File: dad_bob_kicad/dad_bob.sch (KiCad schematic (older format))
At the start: 10 parts, among them J1_BNC1 BNC5-J-P-GN-RA-BH2D, J2_BLACK1 Conn_01x01, J3_RED1 Conn_01x01, T1 GT07-110-013, U1 SL1002A600SP

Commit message: Imported HPF, added divider, dad IO, & relay
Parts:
- added C?: CP, symbol Device:CP
- added D? (x2): 1N4001, Diode_THT:D_DO-41_SOD81_P10.16mm_Horizontal, symbol Diode:1N4001
- added J1, J2: Conn_01x01, symbol Connector_Generic:Conn_01x01
- added J? (x2): analog_discovery_IO, symbol Connector_Generic:analog_discovery_IO
- added K?: EC2-5NU, Relay_THT:Relay_DPDT_Kemet_EC2, symbol Relay:EC2-5NU
- added Q?: 2N2219, Package_TO_SOT_THT:TO-39-3, symbol Transistor_BJT:2N2219
- added R? (x5): 1M, symbol Device:R
- added R?: 50k, symbol Device:R
- added R?: 1k, symbol Device:R
- J3: renamed from J2_BLACK1; footprint Connector_Coaxial:SMA_Amphenol_132203-12_Horizontal -> (none)
- J4: renamed from J3_RED1; footprint Connector_Coaxial:SMA_Amphenol_132203-12_Horizontal -> (none)
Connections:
- net labels added: CV7, CV8, DIVin1+, DIVin1-, DIVout1+, DIVout1-, GND, PLCin+, PLCin-, PLCout+, PLCout-, relaypwr, scope1+, scope1-, scope2+, scope2-, waveform
- net labels removed: Out
- wire segments 41 -> 71
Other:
- moved on the sheet: C1, C2, J1_BNC1, J3, J4, RV1, T1, U1, V1

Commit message: Corrected hpf scheme, added pass throughs on the dad io, changed j1/j2 inputs
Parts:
- removed J?: analog_discovery_IO, symbol Connector_Generic:analog_discovery_IO
- added C?: CP, symbol Device:CP
- added D? (x2): 1N4001, Diode_THT:D_DO-41_SOD81_P10.16mm_Horizontal, symbol Diode:1N4001
- added J?: analog_discovery_IO, symbol Connector_Generic:analog_discovery_IO
- added K?: EC2-5NU, Relay_THT:Relay_DPDT_Kemet_EC2, symbol Relay:EC2-5NU
- added Q?: 2N2219, Package_TO_SOT_THT:TO-39-3, symbol Transistor_BJT:2N2219
- added R? (x2): 1M, symbol Device:R
- added R?: 50k, symbol Device:R
- added R?: 1k, symbol Device:R
- renumbered J1_BNC1 to J7
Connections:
- net labels added: 1, 10, 11, 12, 13, 14, 15, 2, 3, 4, 5, 8, 9, BNCin+, BNCin-, CV6, DIVin2+, DIVin2-, DIVout2+, DIVout2-, V-, trigger1, trigger2, waveform1, waveform2
- net labels removed: CV8, waveform
- wire segments 71 -> 158
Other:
- moved on the sheet: C1, C2, C?, D?, J1, J2, J3, J4, J7, J?, K?, Q?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

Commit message: Reworked voltage divider, added attenuation simulation schematic
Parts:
- removed R? (x2): 50k, symbol Device:R
- removed R? (x4): 1M, symbol Device:R
- added C? (x6): 4pf, symbol Device:C
- added C? (x4): 350pF, symbol Device:C
- added R? (x2): 50k, symbol Device:R
- added R?: DNP, symbol Device:R
- added R? (x3): 1M, symbol Device:R
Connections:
- wire segments 158 -> 183
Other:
- note added: "this tvs needs switched out"
- moved on the sheet: C1, C2, C?, D?, J1, J2, J3, J4, J7, J?, K?, Q?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

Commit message: Altered voltage divider section & added simulation circuit
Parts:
- C2: footprint Capacitor_SMD:C_0603_1608Metric_Pad1.05x0.95mm_HandSolder -> Capacitor_SMD:C_0805_2012Metric_Pad1.15x1.40mm_HandSolder
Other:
- note added: "Make C2 0806"
- note added: "this tvs needs switched out: SMCJ9.0CA"
- note removed: "this tvs needs switched out"
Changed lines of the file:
@@
 F 0 "C2" H 5122 1254 50  0000 R CNN
 F 1 "220pF" H 5122 1345 50  0000 R CNN
-F 2 "Capacitor_SMD:C_0603_1608Metric_Pad1.05x0.95mm_HandSolder" H 5300 1300 50  0001 C CNN
+F 2 "Capacitor_SMD:C_0805_2012Metric_Pad1.15x1.40mm_HandSolder" H 5300 1300 50  0001 C CNN
 F 3 "~" H 5300 1300 50  0001 C CNN
 F 4 "C" H 5300 1300 50  0001 C CNN "Spice_Primitive"
@@
 Wire Wire Line
 	2750 950  3050 950
-Text Notes 4250 1750 0    50   ~ 0
-this tvs needs switched out
 Wire Wire Line
 	1100 5600 1300 5600
@@
 Wire Wire Line
 	2400 6050 2400 6100
+Text Notes 4200 1800 0    50   ~ 0
+this tvs needs switched out: SMCJ9.0CA
+Text Notes 5450 1450 0    50   ~ 0
+Make C2 0806
 $EndSCHEMATC

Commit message: Added differential schematic & associated symbols & footprints, no values, ready for initial layout
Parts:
- removed D1: SMCJ5.0A, DIONM7959X262N, symbol SMCJ5.0A:SMCJ5.0A
- added C? (x3): 86nF, symbol Device:C
- added C? (x2): 4pf, symbol Device:C
- added C? (x2): CTRIM, symbol Device:CTRIM
- added D?: SMCJ9.0CA, DIONM7959X262N, symbol SMCJ5.0A:SMCJ9.0CA
- added J? (x3): Conn_01x03_Male, symbol Connector:Conn_01x03_Male
- added J?: BNC5-J-P-GN-RA-BH2D, BNC5-J-P-GN-RA-BH2D_kicad:BNC5JPGNRABH2D, symbol BNC5-J-P-GN-RA-BH2D:BNC5-J-P-GN-RA-BH2D
- added R? (x3): 30M, symbol Device:R
- added R? (x2): 1M, symbol Device:R
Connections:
- wire segments 183 -> 221
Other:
- note added: "BNC out for standalone"
- note added: "Made C2 0806"
- note added: "switched to: SMCJ9.0CA"
- note removed: "Make C2 0806"
- note removed: "this tvs needs switched out: SMCJ9.0CA"
- moved on the sheet: C1, C2, C?, D?, J1, J2, J3, J4, J7, K?, Q?, R?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

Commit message: Added pcbNew files, block layouts complete
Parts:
- removed J? (x2): analog_discovery_IO, symbol Connector_Generic:analog_discovery_IO
- removed J?: BNC5-J-P-GN-RA-BH2D, BNC5-J-P-GN-RA-BH2D_kicad:BNC5JPGNRABH2D, symbol BNC5-J-P-GN-RA-BH2D:BNC5-J-P-GN-RA-BH2D
- removed V1: dc 0 ac 240, symbol pspice:VSOURCE
- added J6: Conn_02x15_Odd_Even, Connector_PinHeader_2.54mm:PinHeader_2x15_P2.54mm_Horizontal, symbol Connector_Generic:Conn_02x15_Odd_Even
- added J9: Conn_02x15_Odd_Even, Connector_PinSocket_2.54mm:PinSocket_2x15_P2.54mm_Horizontal, symbol Connector_Generic:Conn_02x15_Odd_Even
- C10, C11, C12, C13, C15, C16, C18, C19, C20, C21, C3, C4, C5, C6, C7, C8, C9: renamed from C?; footprint (none) -> Capacitor_SMD:C_0805_2012Metric_Pad1.15x1.40mm_HandSolder
- C14, C17: renamed from C?; footprint (none) -> Capacitor_SMD:C_Trimmer_Voltronics_JQ
- D1: renamed from D?; footprint DIONM7959X262N -> SMCJ5:DIONM7959X262N; symbol SMCJ5.0A:SMCJ9.0CA -> 00_kyuditsky_kicad:SMCJ9.0CA
- J1, J2, J3, J4: footprint (none) -> kyuditsky_kicad_fp:Banana_Jack_S_RA_73099
- J10, J5, J8: renamed from J?; footprint (none) -> Connector_PinHeader_2.54mm:PinHeader_1x03_P2.54mm_Vertical
- J7: symbol BNC5-J-P-GN-RA-BH2D:BNC5-J-P-GN-RA-BH2D -> 00_kyuditsky_kicad:BNC5-J-P-GN-RA-BH2D
- R1, R10, R11, R12, R13, R14, R15, R16, R2, R3, R4, R5, R6, R7, R8, R9: renamed from R?; footprint (none) -> Resistor_SMD:R_0805_2012Metric_Pad1.15x1.40mm_HandSolder
- RV1: footprint CAPPM10080X500N -> VP4032K122R300_kicad:CAPPM10080X500N; symbol VP4032K122R300:VP4032K122R300 -> 00_kyuditsky_kicad:VP4032K122R300
- T1: footprint GT07-110-013-Modifed:GT07110013 -> kyuditsky_kicad_fp:GT07110013; symbol GT07-110-013:GT07-110-013 -> 00_kyuditsky_kicad:GT07-110-013
- U1: symbol SL1002A600SP:SL1002A600SP -> 00_kyuditsky_kicad:SL1002A600SP
- gave numbers to parts that had none: 8
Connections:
- net 0: now also J6.16 (Pin_16), J9.16 (Pin_16)
- net 1: now also J6.18 (Pin_18), J9.18 (Pin_18)
- net 10: now also J6.19 (Pin_19), J9.19 (Pin_19)
- net 11: now also J6.21 (Pin_21), J9.21 (Pin_21)
- net 12: now also J6.23 (Pin_23), J9.23 (Pin_23)
- net 13: now also J6.25 (Pin_25), J9.25 (Pin_25)
- net 14: now also J6.27 (Pin_27), J9.27 (Pin_27)
- net 15: now also J6.29 (Pin_29), J9.29 (Pin_29)
- net 2: now also J6.20 (Pin_20), J9.20 (Pin_20)
- net 3: now also J6.22 (Pin_22), J9.22 (Pin_22)
- net 4: now also J6.24 (Pin_24), J9.24 (Pin_24)
- net 5: now also J6.26 (Pin_26), J9.26 (Pin_26)
- net 8: now also J6.15 (Pin_15), J9.15 (Pin_15)
- net 9: now also J6.17 (Pin_17), J9.17 (Pin_17)
- net BNCin+: now also K2.3; no longer K2.5
- net BNCin-: now also K2.10; no longer K2.8
- net CV6: now also J6.28 (Pin_28), J9.28 (Pin_28)
- net CV7: now also J6.30 (Pin_30), J9.30 (Pin_30)
- net DIVout2+: now also K2.5; no longer K2.3
- net DIVout2-: now also K2.8; no longer K2.10
- net GND: now also J6.11 (Pin_11), J6.12 (Pin_12), J6.5 (Pin_5), J6.6 (Pin_6), J9.11 (Pin_11), J9.12 (Pin_12), J9.5 (Pin_5), J9.6 (Pin_6)
- net relaypwr: now also J6.8 (Pin_8), J9.8 (Pin_8)
- net scope1+: now also J6.2 (Pin_2), J9.2 (Pin_2)
- net scope1-: now also J6.1 (Pin_1), J9.1 (Pin_1)
- net scope2+: now also J6.4 (Pin_4), J9.4 (Pin_4)
- net scope2-: now also J6.3 (Pin_3), J9.3 (Pin_3)
- net trigger1: now also J6.14 (Pin_14), J9.14 (Pin_14)
- net trigger2: now also J6.13 (Pin_13), J9.13 (Pin_13)
- net waveform1: now also J6.10 (Pin_10), J9.10 (Pin_10)
- net waveform2: now also J6.9 (Pin_9), J9.9 (Pin_9)
- new net dad_V-: J6.7 (Pin_7), J9.7 (Pin_7)
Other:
- note removed: "BNC out for standalone"

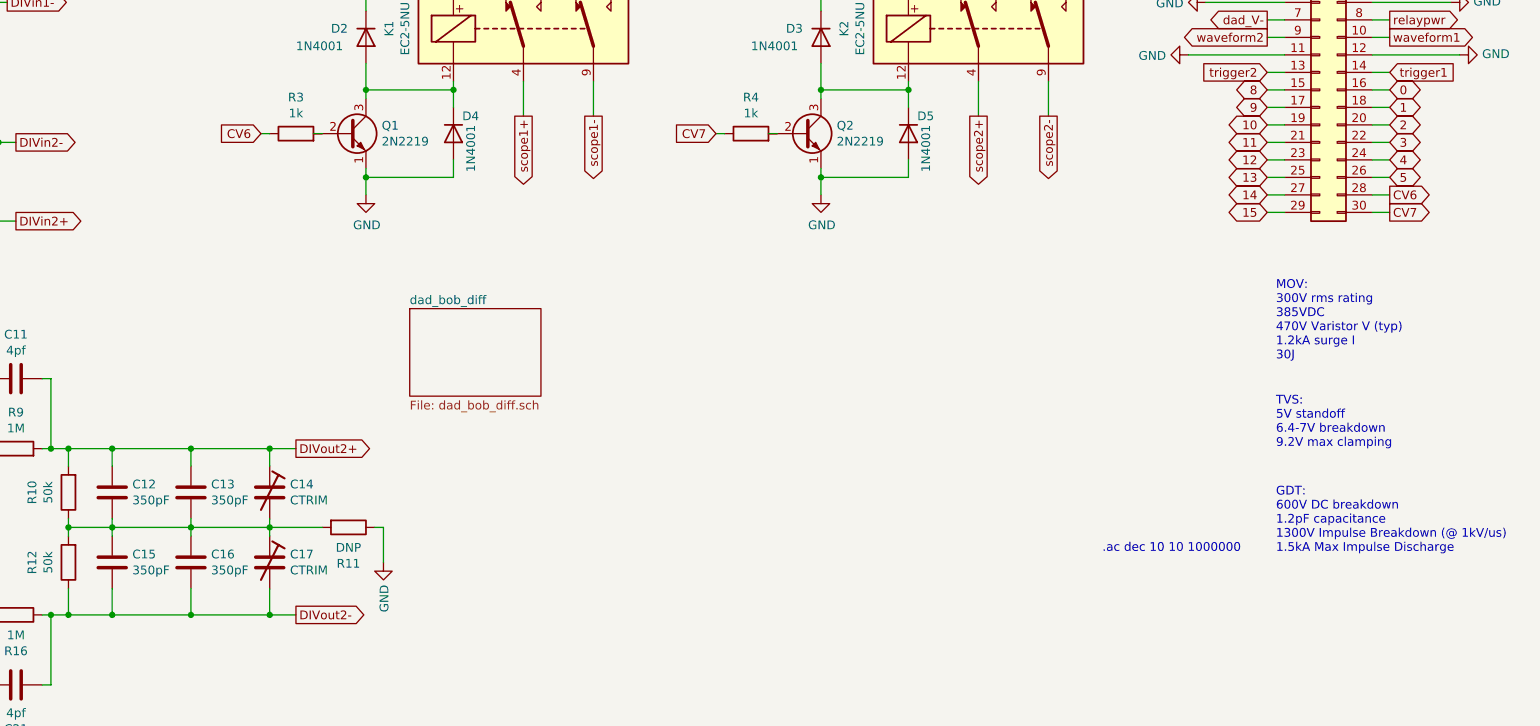
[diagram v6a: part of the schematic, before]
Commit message: changed some layout, realized it needs some rework, but versioning for posterity
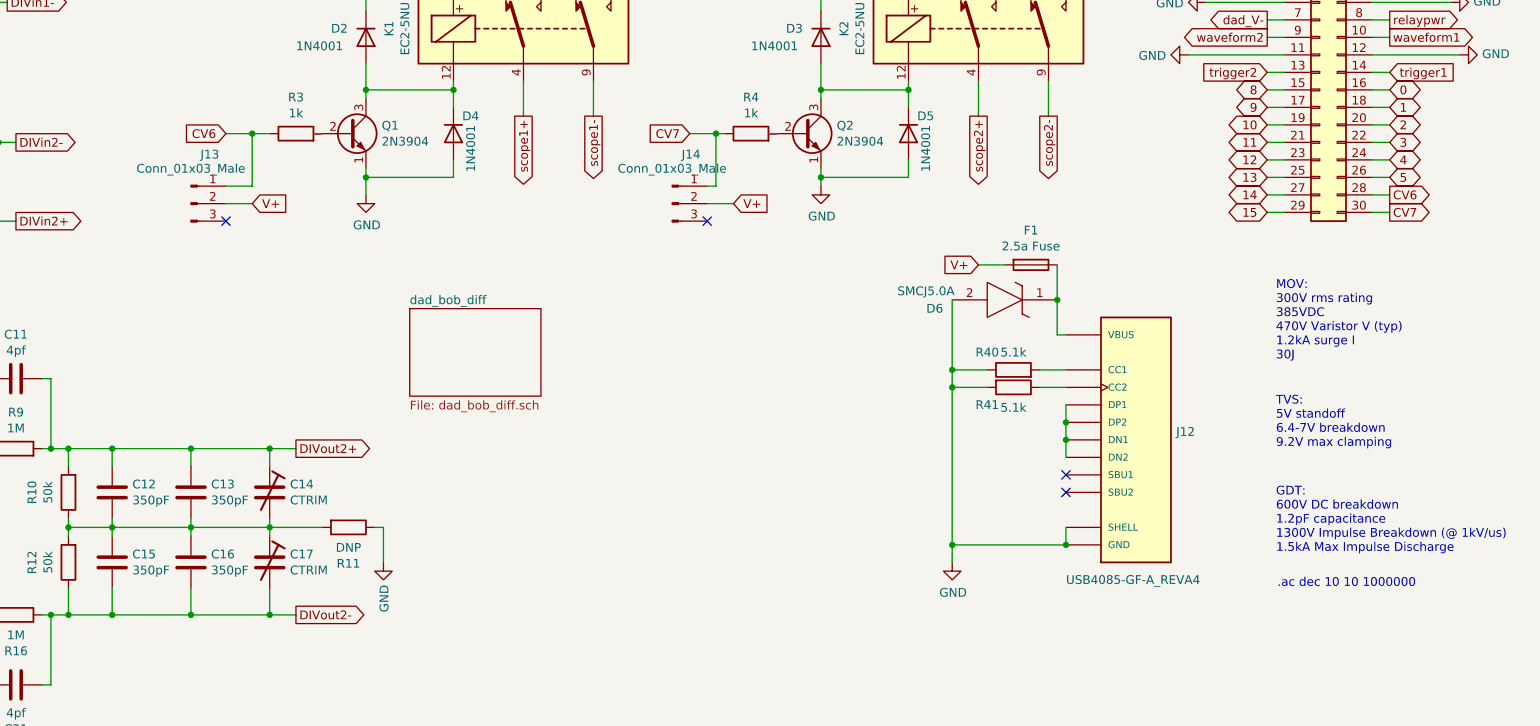
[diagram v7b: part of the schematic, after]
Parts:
- removed Q1, Q2: 2N2219, Package_TO_SOT_THT:TO-39-3, symbol Transistor_BJT:2N2219
- added D6: SMCJ5.0A, kyuditsky_kicad_fp:littlefuseTVS, symbol 00_kyuditsky_kicad:SMCJ5.0A
- added F1: 2.5a Fuse, Resistor_THT:R_Axial_DIN0204_L3.6mm_D1.6mm_P2.54mm_Vertical, symbol Device:Fuse
- added J12: USB4085-GF-A_REVA4, GCT_USB4085-GF-A_REVA4, symbol 00_kyuditsky_kicad:USB4085-GF-A_REVA4
- added J13, J14: Conn_01x03_Male, Connector_PinHeader_2.54mm:PinHeader_1x03_P2.54mm_Vertical, symbol Connector:Conn_01x03_Male
- added Q1, Q2: 2N3904, Package_TO_SOT_THT:TO-92_Inline, symbol Transistor_BJT:2N3904
- added R40, R41: 5.1k, Resistor_SMD:R_0805_2012Metric_Pad1.15x1.40mm_HandSolder, symbol Device:R
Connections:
- net CV6: now also J13.1 (Pin_1)
- net CV7: now also J14.1 (Pin_1)
- net GND: now also D6.2, J12.A1 (GND), J12.A12 (GND), J12.B1 (GND), J12.B12 (GND), J12.P1 (SHELL), J12.P2 (SHELL), J12.P3 (SHELL), J12.P4 (SHELL), Q1.1 (E), Q2.1 (E), R40.1, R41.2
- net at D2.2 (A), D4.1 (K), K1.12: now also Q1.3 (C)
- net at R3.2: now also Q1.2 (B)
- net at R4.2: now also Q2.2 (B)
- net at D3.2 (A), D5.1 (K), K2.12: now also Q2.3 (C)
- new net: J12.A5 (CC1), R40.2
- new net: J12.B5 (CC2), R41.1
- new net: D6.1, F1.1, J12.A4 (VBUS), J12.A9 (VBUS), J12.B4 (VBUS), J12.B9 (VBUS)
- new net: J12.A6 (DP1), J12.A7 (DN1), J12.B6 (DP2), J12.B7 (DN2)
- new net V+: F1.2, J13.2 (Pin_2), J14.2 (Pin_2)
- no-connect marks 2 -> 6
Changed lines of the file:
@@
 Wire Wire Line
 	6700 1200 6700 1550
-Text Notes 9300 6200 2    50   ~ 0
+Text Notes 10300 6400 2    50   ~ 0
 .ac dec 10 10 1000000
-$Comp
-L Transistor_BJT:2N2219 Q1
-U 1 1 620C8AE8
-P 4200 3800
-F 0 "Q1" H 4390 3846 50  0000 L CNN
-F 1 "2N2219" H 4390 3755 50  0000 L CNN
-F 2 "Package_TO_SOT_THT:TO-39-3" H 4400 3725 50  0001 L CIN
-F 3 "http://www.onsemi.com/pub_link/Collateral/2N2219-D.PDF" H 4200 3800 50  0001 L CNN
-	1    4200 3800
-	1    0    0    -1
-$EndComp
 $Comp
 L Device:R R7
@@
 Wire Wire Line
 	5200 3700 5200 3500
-Text GLabel 3700 3800 0    50   Input ~ 0
+Text GLabel 3500 3800 0    50   Input ~ 0
 CV6
 Wire Wire Line
-	3700 3800 3750 3800
+	3500 3800 3650 3800
 $Comp
 L Diode:1N4001 D2
@@
 	2150 3050 2150 2850
 $Comp
-L Transistor_BJT:2N2219 Q2
-U 1 1 622492C8
-P 6800 3800
-F 0 "Q2" H 6990 3846 50  0000 L CNN
-F 1 "2N2219" H 6990 3755 50  0000 L CNN
-F 2 "Package_TO_SOT_THT:TO-39-3" H 7000 3725 50  0001 L CIN
-F 3 "http://www.onsemi.com/pub_link/Collateral/2N2219-D.PDF" H 6800 3800 50  0001 L CNN
-	1    6800 3800
-	1    0    0    -1
-$EndComp
-$Comp
 L Relay:EC2-5NU K2
 U 1 1 622492CE
@@
 	7800 3700 7800 3500
 Wire Wire Line
-	6300 3800 6350 3800
+	6150 3800 6300 3800
 $Comp
 L Diode:1N4001 D3
@@
 L power:GND #PWR012
 U 1 1 622492EF
-P 6900 4150
-F 0 "#PWR012" H 6900 3900 50  0001 C CNN
-F 1 "GND" H 6905 3977 50  0000 C CNN
-F 2 "" H 6900 4150 50  0001 C CNN
-F 3 "" H 6900 4150 50  0001 C CNN
-	1    6900 4150
+P 6900 4100
+F 0 "#PWR012" H 6900 3850 50  0001 C CNN
+F 1 "GND" H 6905 3927 50  0000 C CNN
+F 2 "" H 6900 4100 50  0001 C CNN
+F 3 "" H 6900 4100 50  0001 C CNN
+	1    6900 4100
 	1    0    0    -1
 $EndComp
@@
 Wire Wire Line
 	7400 4050 6900 4050
-Connection ~ 6900 4050
-Wire Wire Line
-	6900 4050 6900 4150
 Wire Wire Line
 	6900 3400 6900 3550
@@
 Wire Wire Line
 	7700 2700 7700 2900
-Text GLabel 6300 3800 0    50   Input ~ 0
+Text GLabel 6150 3800 0    50   Input ~ 0
 CV7
 Text GLabel 7700 2700 1    50   Input ~ 0
@@
 	1    0    0    -1
 $EndComp
+$Comp
+L Device:R R40
+U 1 1 62530B7C
+P 8000 5150
+F 0 "R40" V 8100 5300 50  0000 C CNN
+F 1 "5.1k" V 8100 5150 50  0000 C CNN
+F 2 "Resistor_SMD:R_0805_2012Metric_Pad1.15x1.40mm_HandSolder" V 7930 5150 50  0001 C CNN
+F 3 "~" H 8000 5150 50  0001 C CNN
+	1    8000 5150
+	0    -1   -1   0
+$EndComp
+$Comp
+L Device:R R41
+U 1 1 62542233
+P 8000 5250
+F 0 "R41" V 8100 5100 50  0000 C CNN
+F 1 "5.1k" V 8116 5250 50  0000 C CNN
+F 2 "Resistor_SMD:R_0805_2012Metric_Pad1.15x1.40mm_HandSolder" V 7930 5250 50  0001 C CNN
+F 3 "~" H 8000 5250 50  0001 C CNN
+	1    8000 5250
+	0    1    1    0
+$EndComp
+Text GLabel 7800 4550 0    50   Input ~ 0
+V+
+$Comp
+L Device:Fuse F1
+U 1 1 626099AA
+P 8100 4550
+F 0 "F1" V 7903 4550 50  0000 C CNN
+F 1 "2.5a Fuse" V 7994 4550 50  0000 C CNN
+F 2 "Resistor_THT:R_Axial_DIN0204_L3.6mm_D1.6mm_P2.54mm_Vertical" V 8030 4550 50  0001 C CNN
+F 3 "~" H 8100 4550 50  0001 C CNN
+	1    8100 4550
+	0    1    1    0
+$EndComp
+$Comp
+L power:GND #PWR014
+U 1 1 62690EAA
+P 7650 6250
+F 0 "#PWR014" H 7650 6000 50  0001 C CNN
+F 1 "GND" H 7655 6077 50  0000 C CNN
+F 2 "" H 7650 6250 50  0001 C CNN
+F 3 "" H 7650 6250 50  0001 C CNN
+	1    7650 6250
+	1    0    0    -1
+$EndComp
+$Comp
+L Transistor_BJT:2N3904 Q1
+U 1 1 626BD250
+P 4200 3800
+F 0 "Q1" H 4390 3846 50  0000 L CNN
+F 1 "2N3904" H 4390 3755 50  0000 L CNN
+F 2 "Package_TO_SOT_THT:TO-92_Inline" H 4400 3725 50  0001 L CIN
+F 3 "https://www.fairchildsemi.com/datasheets/2N/2N3904.pdf" H 4200 3800 50  0001 L CNN
+	1    4200 3800
+	1    0    0    -1
+$EndComp
+$Comp
+L Transistor_BJT:2N3904 Q2
+U 1 1 626BEF9F
+P 6800 3800
+F 0 "Q2" H 6990 3846 50  0000 L CNN
+F 1 "2N3904" H 6990 3755 50  0000 L CNN
+F 2 "Package_TO_SOT_THT:TO-92_Inline" H 7000 3725 50  0001 L CIN
+F 3 "https://www.fairchildsemi.com/datasheets/2N/2N3904.pdf" H 6800 3800 50  0001 L CNN
+	1    6800 3800
+	1    0    0    -1
+$EndComp
+$Comp
+L 00_kyuditsky_kicad:SMCJ5.0A D6
+U 1 1 625E9666
+P 8250 4750
+F 0 "D6" H 8950 4800 50  0000 C CNN
+F 1 "SMCJ5.0A" H 9000 4700 50  0000 C CNN
+F 2 "kyuditsky_kicad_fp:littlefuseTVS" H 8650 4900 50  0001 L BNN
+F 3 "https://componentsearchengine.com/Datasheets/2/SMCJ5.0A.pdf" H 8650 4800 50  0001 L BNN
+F 4 "ESD Suppressors / TVS Diodes 1.5kW 5V 5% Uni-Directional" H 8650 4700 50  0001 L BNN "Description"
+F 5 "2.62" H 8650 4600 50  0001 L BNN "Height"
+F 6 "576-SMCJ5.0A" H 8650 4500 50  0001 L BNN "Mouser Part Number"
+F 7 "https://www.mouser.co.uk/ProductDetail/Littelfuse/SMCJ50A?qs=HR2RnyOI4E4RumofpgUEcw%3D%3D" H 8650 4400 50  0001 L BNN "Mouser Price/Stock"
+F 8 "LITTELFUSE" H 8650 4300 50  0001 L BNN "Manufacturer_Name"
+F 9 "SMCJ5.0A" H 8650 4200 50  0001 L BNN "Manufacturer_Part_Number"
+	1    8250 4750
+	-1   0    0    1
+$EndComp
+$Comp
+L 00_kyuditsky_kicad:USB4085-GF-A_REVA4 J12
+U 1 1 625FD762
+P 8700 5550
+F 0 "J12" H 8930 5596 50  0000 L CNN
+F 1 "USB4085-GF-A_REVA4" H 8300 4750 50  0000 L CNN
+F 2 "GCT_USB4085-GF-A_REVA4" H 8700 5550 50  0001 L BNN
+F 3 "" H 8700 5550 50  0001 L BNN
+F 4 "A4" H 8700 5550 50  0001 L BNN "PARTREV"
+F 5 "3.46mm" H 8700 5550 50  0001 L BNN "MAXIMUM_PACKAGE_HEIGHT"
+F 6 "Global Connector Technology" H 8700 5550 50  0001 L BNN "MANUFACTURER"
+F 7 "Manufacturer Recommendations" H 8700 5550 50  0001 L BNN "STANDARD"
+	1    8700 5550
+	1    0    0    -1
+$EndComp
+Wire Wire Line
+	6900 4100 6900 4050
+Connection ~ 6900 4050
+Wire Wire Line
+	8250 4550 8250 4750
+Wire Wire Line
+	8300 4950 8250 4950
+Wire Wire Line
+	8250 4950 8250 4750
+Connection ~ 8250 4750
+Wire Wire Line
+	7950 4550 7800 4550
+Wire Wire Line
+	7650 4750 7650 5150
+Wire Wire Line
+	7850 5150 7650 5150
+Connection ~ 7650 5150
+Wire Wire Line
+	7650 5150 7650 5250
+Wire Wire Line
+	7850 5250 7650 5250
+Connection ~ 7650 5250
+Wire Wire Line
+	7650 5250 7650 6150
+Wire Wire Line
+	8150 5150 8300 5150
+Wire Wire Line
+	8150 5250 8300 5250
+Wire Wire Line
+	8300 6150 7650 6150
+Connection ~ 7650 6150
+Wire Wire Line
+	7650 6150 7650 6250
+Wire Wire Line
+	8300 6050 8300 6150
+Connection ~ 8300 6150
+Wire Wire Line
+	8300 5350 8300 5450
+Connection ~ 8300 5450
+Wire Wire Line
+	8300 5450 8300 5550
+Connection ~ 8300 5550
+Wire Wire Line
+	8300 5550 8300 5650
+NoConn ~ 8300 5750
+NoConn ~ 8300 5850
+$Comp
+L Connector:Conn_01x03_Male J13
+U 1 1 627F2D97
+P 3300 4200
+F 0 "J13" H 3408 4481 50  0000 C CNN
+F 1 "Conn_01x03_Male" H 3300 4400 50  0000 C CNN
+F 2 "Connector_PinHeader_2.54mm:PinHeader_1x03_P2.54mm_Vertical" H 3300 4200 50  0001 C CNN
+F 3 "~" H 3300 4200 50  0001 C CNN
+	1    3300 4200
+	1    0    0    -1
+$EndComp
+Wire Wire Line
+	3500 4100 3650 4100
+Wire Wire Line
+	3650 4100 3650 3800
+Connection ~ 3650 3800
+Wire Wire Line
+	3650 3800 3750 3800
+NoConn ~ 3500 4300
+Text GLabel 3650 4200 2    50   Input ~ 0
+V+
+Wire Wire Line
+	3650 4200 3500 4200
+$Comp
+L Connector:Conn_01x03_Male J14
+U 1 1 62827F7F
+P 6050 4200
+F 0 "J14" H 6158 4481 50  0000 C CNN
+F 1 "Conn_01x03_Male" H 6050 4400 50  0000 C CNN
+F 2 "Connector_PinHeader_2.54mm:PinHeader_1x03_P2.54mm_Vertical" H 6050 4200 50  0001 C CNN
+F 3 "~" H 6050 4200 50  0001 C CNN
+	1    6050 4200
+	1    0    0    -1
+$EndComp
+Wire Wire Line
+	6250 4100 6300 4100
+Wire Wire Line
+	6300 4100 6300 3800
+Connection ~ 6300 3800
+Wire Wire Line
+	6300 3800 6350 3800
+NoConn ~ 6250 4300
+Text GLabel 6400 4200 2    50   Input ~ 0
+V+
+Wire Wire Line
+	6400 4200 6250 4200
 $EndSCHEMATC
